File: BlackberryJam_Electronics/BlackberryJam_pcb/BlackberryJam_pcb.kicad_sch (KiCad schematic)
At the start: 13 parts

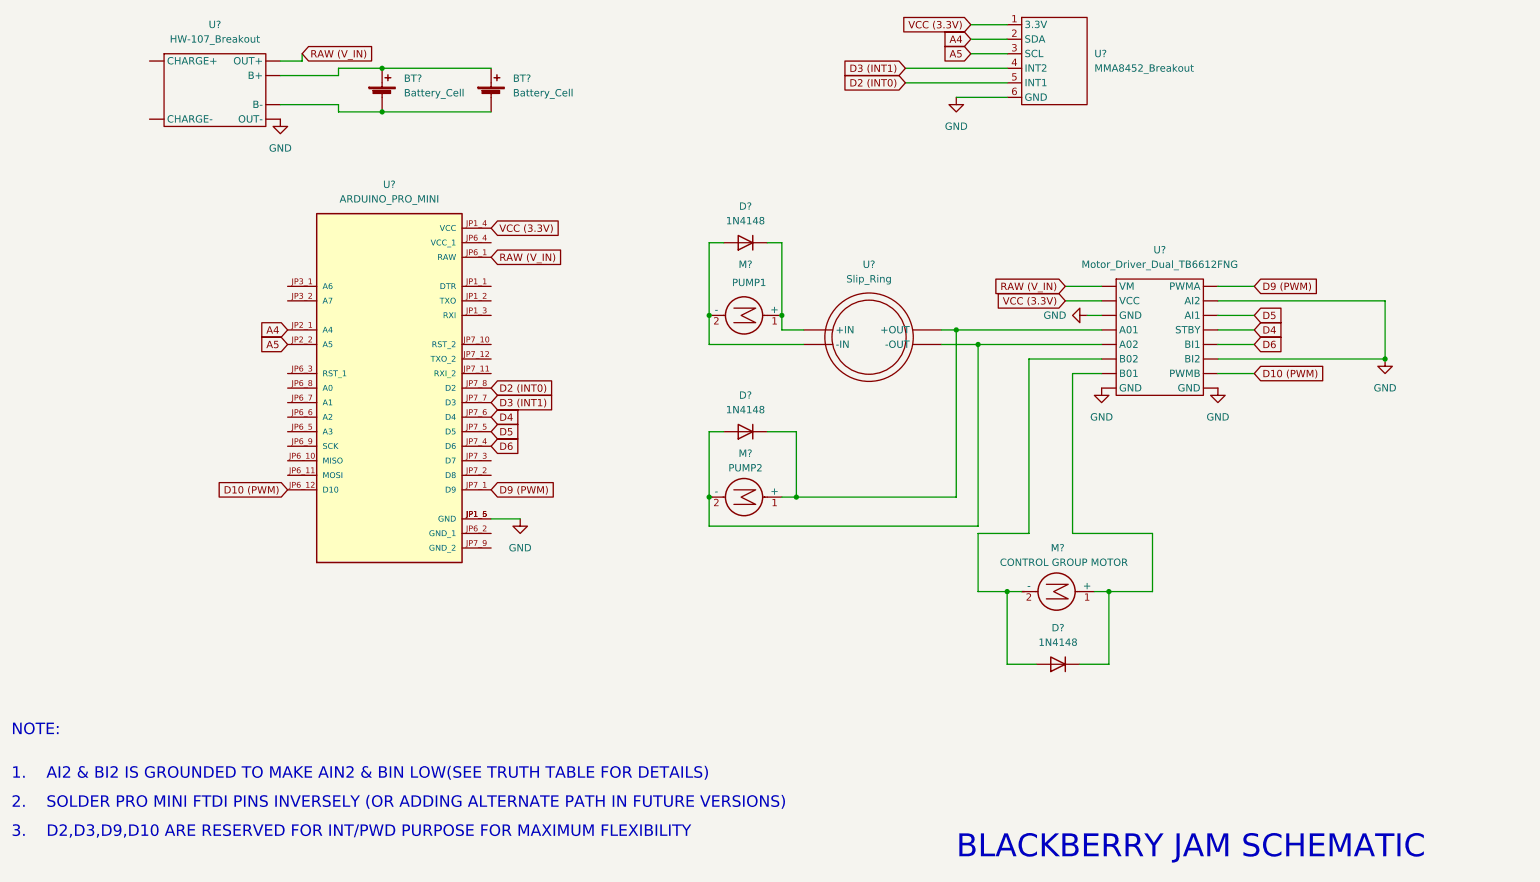
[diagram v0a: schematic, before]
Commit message: Updated Library Path
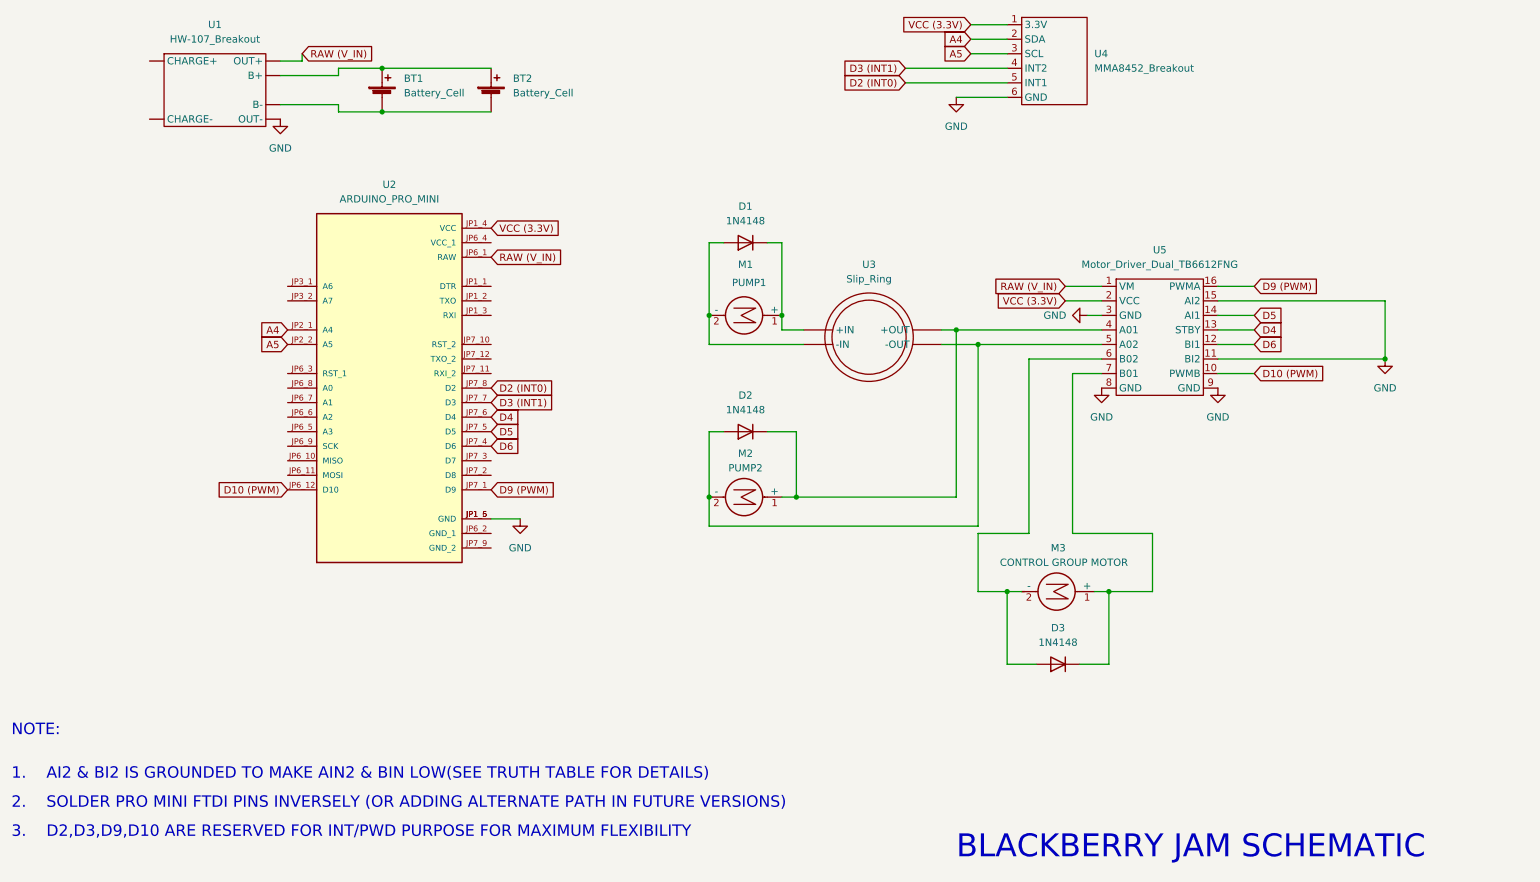
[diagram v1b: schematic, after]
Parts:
- U5: renamed from U?; footprint (none) -> BlackberryJam_footprint:Dual_Motor_Driver
- gave numbers to parts that had none: 12
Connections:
- net D10 (PWM): now also U5.10 (PWMB); no longer U5. (VM)
- net D4: now also U5.13 (STBY); no longer U5. (VM)
- net D5: now also U5.14 (AI1); no longer U5. (VM)
- net D6: now also U5.12 (BI1); no longer U5. (VM)
- net D9 (PWM): now also U5.16 (PWMA); no longer U5. (VM)
- net GND: now also U5.11 (BI2), U5.15 (AI2), U5.3 (GND), U5.8 (GND), U5.9 (GND); no longer U5. (VM)
- net RAW (V_IN): now also U5.1 (VM); no longer U5. (VM)
- net VCC (3.3V): now also U5.2 (VCC); no longer U5. (VM)
- net at D3.1 (K), M3.1 (+): now also U5.7 (B01); no longer U5. (VM)
- net at D3.2 (A), M3.2 (-): now also U5.6 (B02); no longer U5. (VM)
- net at D2.1 (K), M2.1 (+), U3. (-OUT): now also U5.4 (A01); no longer U5. (VM)
- net at D2.2 (A), M2.2 (-), U3. (-OUT): now also U5.5 (A02); no longer U5. (VM)

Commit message: PCB Layout with components
1. Updated and assigned footprints in schematic
2. Placed components on PCB editor

Note:
No connection is made in the PCB now
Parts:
- M2, M3, U1, U3: footprint (none) -> Connector_PinHeader_2.54mm:PinHeader_1x02_P2.54mm_Vertical
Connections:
- net GND: now also U1.6 (OUT-); no longer U1. (OUT-)
- net RAW (V_IN): now also U1.5 (OUT+); no longer U1. (OUT-)
- net at D2.1 (K), M2.1 (+), U5.4 (A01): now also D1.2 (A), U3.2 (-IN); no longer U3. (-OUT)
- net at D2.2 (A), M2.2 (-), U5.5 (A02): now also D1.1 (K), U3.1 (+IN); no longer U3. (-OUT)
- net at BT1.1 (+), BT2.1 (+): now also U1.3 (B+); no longer U1. (OUT-)
- net at BT1.2 (-), BT2.2 (-): now also U1.4 (B-); no longer U1. (OUT-)
- new net: M1.1 (+), U3.3 (+OUT)
- new net: M1.2 (-), U3.4 (-OUT)
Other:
- note added: "1. AI2 & BI2 IS GROUNDED TO MAKE AIN2 & BIN2 LOW(SEE TRUTH TABLE FOR DETAILS)"
- note added: "3. D2,D3,D9,D10 ARE RESERVED FOR INT/PWM PURPOSE FOR MAXIMUM FLEXIBILITY"
- note removed: "1. AI2 & BI2 IS GROUNDED TO MAKE AIN2 & BIN LOW(SEE TRUTH TABLE FOR DETAILS)"
- note removed: "3. D2,D3,D9,D10 ARE RESERVED FOR INT/PWD PURPOSE FOR MAXIMUM FLEXIBILITY"
- moved on the sheet: D1, D3, M1, M3

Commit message: SCH and PCB Update
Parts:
- removed D2: 1N4148, Diode_THT:D_DO-35_SOD27_P7.62mm_Horizontal, symbol Diode:1N4148
- D1: footprint Diode_THT:D_DO-35_SOD27_P7.62mm_Horizontal -> Diode_SMD:D_0805_2012Metric
- D2: renamed from D3; footprint Diode_THT:D_DO-35_SOD27_P7.62mm_Horizontal -> Diode_SMD:D_0805_2012Metric
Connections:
- net at D1.2 (A), U3.2 (-IN), U5.4 (A01): now also M2.2 (-); no longer M2.1 (+)
- net at D1.1 (K), U3.1 (+IN), U5.5 (A02): now also M2.1 (+); no longer M2.2 (-)
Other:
- moved on the sheet: M2
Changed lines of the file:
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@@
   (junction (at 186.69 83.82) (diameter 0) (color 0 0 0 0)
   )
-  (junction (at 143.51 113.03) (diameter 0) (color 0 0 0 0)
-  )
   (junction (at 196.85 129.54) (diameter 0) (color 0 0 0 0)
   )
-  (junction (at 158.75 113.03) (diameter 0) (color 0 0 0 0)
-  )
   (wire (pts (xy 86.36 45.72) (xy 105.41 45.72))
     (stroke (width 0) (type default) (color 0 0 0 0))
@@
     (stroke (width 0) (type default) (color 0 0 0 0))
   )
-  (wire (pts (xy 156.21 113.03) (xy 158.75 113.03))
-    (stroke (width 0) (type default) (color 0 0 0 0))
-  )
   (wire (pts (xy 166.37 81.28) (xy 171.45 81.28))
     (stroke (width 0) (type default) (color 0 0 0 0))
@@
     (stroke (width 0) (type default) (color 0 0 0 0))
   )
+  (wire (pts (xy 156.21 107.95) (xy 186.69 107.95))
+    (stroke (width 0) (type default) (color 0 0 0 0))
+  )
   (wire (pts (xy 232.41 91.44) (xy 238.76 91.44))
     (stroke (width 0) (type default) (color 0 0 0 0))
   )
-  (wire (pts (xy 146.05 101.6) (xy 143.51 101.6))
-    (stroke (width 0) (type default) (color 0 0 0 0))
-  )
   (wire (pts (xy 105.41 116.84) (xy 110.49 116.84))
     (stroke (width 0) (type default) (color 0 0 0 0))
   )
-  (wire (pts (xy 143.51 113.03) (xy 143.51 118.11))
-    (stroke (width 0) (type default) (color 0 0 0 0))
-  )
   (wire (pts (xy 78.74 39.37) (xy 78.74 38.1))
     (stroke (width 0) (type default) (color 0 0 0 0))
@@
     (stroke (width 0) (type default) (color 0 0 0 0))
   )
-  (wire (pts (xy 153.67 101.6) (xy 158.75 101.6))
-    (stroke (width 0) (type default) (color 0 0 0 0))
-  )
   (wire (pts (xy 189.23 30.48) (xy 195.58 30.48))
     (stroke (width 0) (type default) (color 0 0 0 0))
   )
-  (wire (pts (xy 158.75 101.6) (xy 158.75 113.03))
-    (stroke (width 0) (type default) (color 0 0 0 0))
-  )
   (wire (pts (xy 72.39 36.83) (xy 72.39 35.56))
     (stroke (width 0) (type default) (color 0 0 0 0))
@@
     (stroke (width 0) (type default) (color 0 0 0 0))
   )
+  (wire (pts (xy 143.51 107.95) (xy 143.51 118.11))
+    (stroke (width 0) (type default) (color 0 0 0 0))
+  )
   (wire (pts (xy 238.76 86.36) (xy 232.41 86.36))
     (stroke (width 0) (type default) (color 0 0 0 0))
@@
     (stroke (width 0) (type default) (color 0 0 0 0))
   )
-  (wire (pts (xy 186.69 113.03) (xy 186.69 83.82))
-    (stroke (width 0) (type default) (color 0 0 0 0))
-  )
-  (wire (pts (xy 158.75 113.03) (xy 186.69 113.03))
+  (wire (pts (xy 186.69 83.82) (xy 186.69 107.95))
     (stroke (width 0) (type default) (color 0 0 0 0))
   )
@@
   )
   (wire (pts (xy 171.45 88.9) (xy 190.5 88.9))
-    (stroke (width 0) (type default) (color 0 0 0 0))
-  )
-  (wire (pts (xy 143.51 101.6) (xy 143.51 113.03))
     (stroke (width 0) (type default) (color 0 0 0 0))
   )
@@
   (symbol (lib_id "Diode:1N4148") (at 205.74 142.24 180) (unit 1)
     (in_bom yes) (on_board yes) (fields_autoplaced)
-    (property "Reference" "D3" (id 0) (at 205.74 135.89 0))
+    (property "Reference" "D2" (id 0) (at 205.74 135.89 0))
     (property "Value" "1N4148" (id 1) (at 205.74 138.43 0))
-    (property "Footprint" "Diode_THT:D_DO-35_SOD27_P7.62mm_Horizontal" (id 2) (at 205.74 137.795 0)
+    (property "Footprint" "Diode_SMD:D_0805_2012Metric" (id 2) (at 205.74 137.795 0)
       (effects (font (size 1.27 1.27)) hide)
     )
@@
     )
     (pin "1")
-  )
-  (symbol (lib_id "Diode:1N4148") (at 149.86 101.6 180) (unit 1)
-    (in_bom yes) (on_board yes) (fields_autoplaced)
-    (property "Reference" "D2" (id 0) (at 149.86 95.25 0))
-    (property "Value" "1N4148" (id 1) (at 149.86 97.79 0))
-    (property "Footprint" "Diode_THT:D_DO-35_SOD27_P7.62mm_Horizontal" (id 2) (at 149.86 97.155 0)
-      (effects (font (size 1.27 1.27)) hide)
-    )
-    (property "Datasheet" "https://assets.nexperia.com/documents/data-sheet/1N4148_1N4448.pdf" (id 3) (at 149.86 101.6 0)
-      (effects (font (size 1.27 1.27)) hide)
-    )
-    (pin "1")
-    (pin "2")
   )
   (symbol (lib_id "Device:Battery_Cell") (at 105.41 43.18 0) (unit 1)
@@
     (pin "2")
   )
-  (symbol (lib_id "Motor:Motor_DC") (at 151.13 113.03 270) (mirror x) (unit 1)
+  (symbol (lib_id "Motor:Motor_DC") (at 148.59 107.95 90) (mirror x) (unit 1)
     (in_bom yes) (on_board yes)
-    (property "Reference" "M2" (id 0) (at 149.86 105.41 90))
-    (property "Value" "PUMP2" (id 1) (at 149.86 107.95 90))
-    (property "Footprint" "Connector_PinHeader_2.54mm:PinHeader_1x02_P2.54mm_Vertical" (id 2) (at 148.844 113.03 0)
-      (effects (font (size 1.27 1.27)) hide)
-    )
-    (property "Datasheet" "~" (id 3) (at 148.844 113.03 0)
+    (property "Reference" "M2" (id 0) (at 149.86 115.57 90))
+    (property "Value" "PUMP2" (id 1) (at 149.86 113.03 90))
+    (property "Footprint" "Connector_PinHeader_2.54mm:PinHeader_1x02_P2.54mm_Vertical" (id 2) (at 150.876 107.95 0)
+      (effects (font (size 1.27 1.27)) hide)
+    )
+    (property "Datasheet" "~" (id 3) (at 150.876 107.95 0)
       (effects (font (size 1.27 1.27)) hide)
     )
@@
       (effects (font (size 1.27 1.27)) (justify right))
     )
-    (property "Footprint" "Diode_THT:D_DO-35_SOD27_P7.62mm_Horizontal" (id 2) (at 175.895 85.09 0)
+    (property "Footprint" "Diode_SMD:D_0805_2012Metric" (id 2) (at 175.895 85.09 0)
       (effects (font (size 1.27 1.27)) hide)
     )
@@
     )
     (path "/d899032e-9784-4c0c-bcda-e65674f5560b"
-      (reference "D1") (unit 1) (value "1N4148") (footprint "Diode_THT:D_DO-35_SOD27_P7.62mm_Horizontal")
-    )
-    (path "/0c0c5c9c-f17e-4817-bf4d-c4b5d6d230f6"
-      (reference "D2") (unit 1) (value "1N4148") (footprint "Diode_THT:D_DO-35_SOD27_P7.62mm_Horizontal")
+      (reference "D1") (unit 1) (value "1N4148") (footprint "Diode_SMD:D_0805_2012Metric")
     )
     (path "/02a1b6c2-6f88-48c7-b7fb-001d925f6edf"
-      (reference "D3") (unit 1) (value "1N4148") (footprint "Diode_THT:D_DO-35_SOD27_P7.62mm_Horizontal")
+      (reference "D2") (unit 1) (value "1N4148") (footprint "Diode_SMD:D_0805_2012Metric")
     )
     (path "/cd2f8b2b-6f46-4bcf-8ef1-ae7fe9565df6"
